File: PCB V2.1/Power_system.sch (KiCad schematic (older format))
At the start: 26 parts, among them J3 B2B-PH-K-S(LF)(SN), J4 B3B-PH-K-S(LF)(SN), Q1 DMG2307L-7, Q2 DMG2307L-7, U2 BQ24210DQCT, U3 AZ1117CR-3.3TRG1_1

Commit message: Images
Images added and organized
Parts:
- added TP35, TP36: TEST_POINT, PCB_Footprints:TEST_POINT, symbol TEST_POINT
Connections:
- wire segments 50 -> 52
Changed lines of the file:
@@
 	5850 2425 5850 3100
 Connection ~ 5850 3100
+$Comp
+L TEST_POINT TP36
+U 1 1 57F5132B
+P 10600 2525
+F 0 "TP36" V 10775 2475 60  0000 L CNN
+F 1 "TEST_POINT" H 10450 2425 60  0000 L CNN
+F 2 "PCB_Footprints:TEST_POINT" H 10775 2800 60  0001 C CNN
+F 3 "" H 10675 2525 60  0001 C CNN
+	1    10600 2525
+	0    -1   -1   0
+$EndComp
+$Comp
+L TEST_POINT TP35
+U 1 1 57F51C69
+P 10150 3700
+F 0 "TP35" V 10325 3650 60  0000 L CNN
+F 1 "TEST_POINT" H 10000 3600 60  0000 L CNN
+F 2 "PCB_Footprints:TEST_POINT" H 10325 3975 60  0001 C CNN
+F 3 "" H 10225 3700 60  0001 C CNN
+	1    10150 3700
+	1    0    0    -1
+$EndComp
+Wire Wire Line
+	10025 3700 10025 3350
+Connection ~ 10025 3350
+Wire Wire Line
+	10600 2650 10600 2900
+Connection ~ 10600 2900
 $EndSCHEMATC

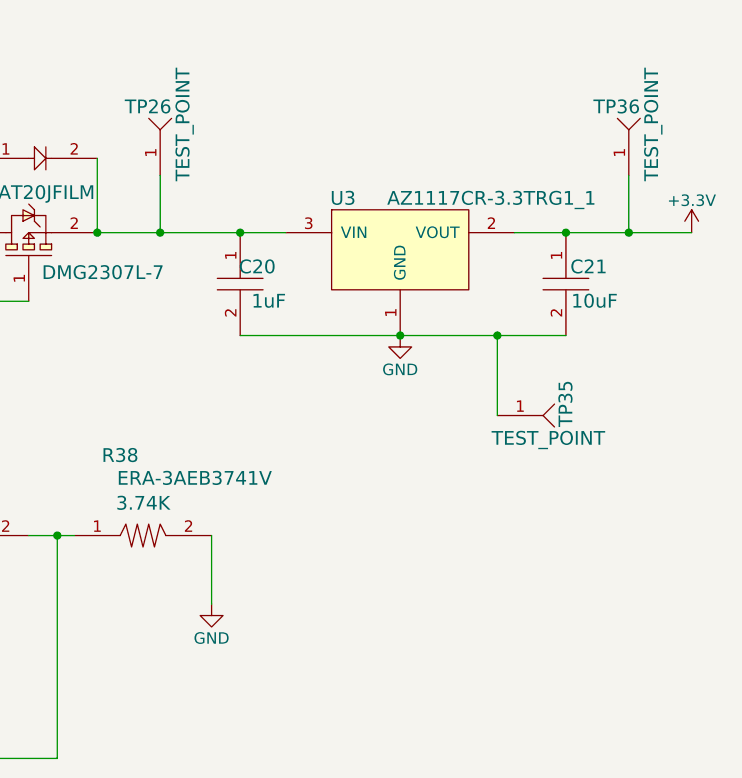
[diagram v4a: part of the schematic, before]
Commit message: LDO and Switch
LDO swapped out for one that better matches the complete system's
amperage requirements. The LDO is now a 600mA one and has a toggle
switch for shuttingit on and off, this will allow the SunLeaf to be
stored and or shipped.
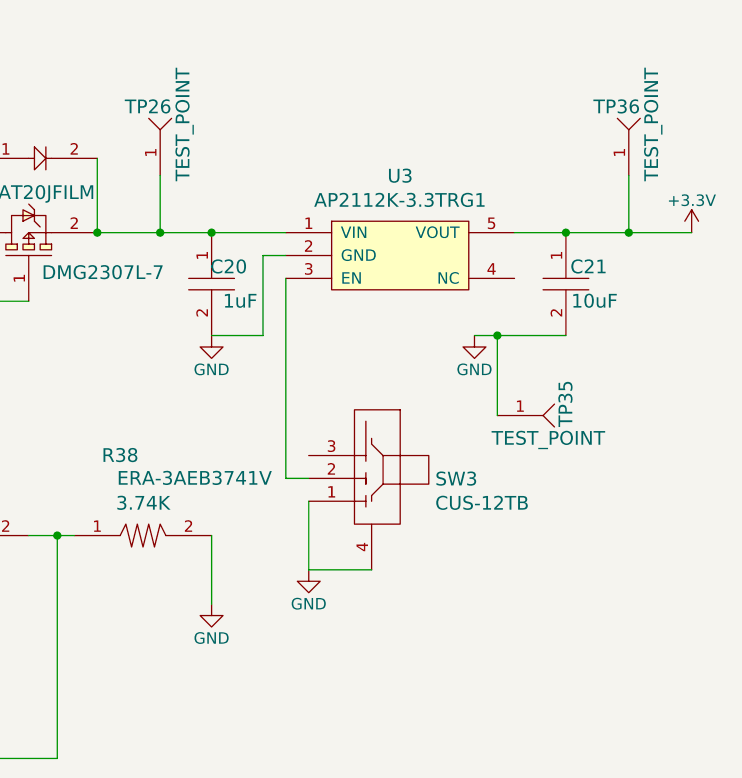
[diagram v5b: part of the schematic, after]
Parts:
- removed U3: AZ1117CR-3.3TRG1_1, PCB_Footprints:AZ1117CR-3.3TRG1, symbol AZ1117CR-3.3TRG1_1
- added SW3: CUS-12TB, PCB_Footprints:CUS-12TB, symbol CUS-12TB
- added U3: AP2112K-3.3TRG1, PCB_Footprints:AP2112K-3.3TRG1, symbol AP2112K-3.3TRG1
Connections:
- wire segments 52 -> 59
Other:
- moved on the sheet: C20
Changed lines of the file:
@@
 L CL05A105KA5NQNC C20
 U 1 1 57D7E6BF
-P 8900 3125
-F 0 "C20" V 8825 3200 60  0000 C CNN
-F 1 "CL05A105KA5NQNC" H 8600 2975 60  0001 C CNN
-F 2 "PCB_Footprints:C0402" H 8150 3175 60  0001 C CNN
-F 3 "http://www.samsungsem.com/kr/support/product-search/mlcc/__icsFiles/afieldfile/2016/08/18/S_CL05A105KA5NQNC.pdf" H 8250 3275 60  0001 C CNN
-F 4 "0.05618 @ 5000" H 8350 3375 60  0001 C CNN "Cost"
-F 5 "5 Sept 2016" H 8450 3475 60  0001 C CNN "Date Created"
-F 6 "5 Sept 2016" H 8550 3575 60  0001 C CNN "Date Modifed"
-F 7 "Adam Vadala-Roth" H 8650 3675 60  0001 C CNN "Designer"
-F 8 "0.55mm" H 8750 3775 60  0001 C CNN "Height"
-F 9 "Yes" H 8850 3875 60  0001 C CNN "RHoS?"
-F 10 "Samsung Electro-Mechanics America, Inc." H 8950 3975 60  0001 C CNN "MFR"
-F 11 "CL05A105KA5NQNC" H 9050 4075 60  0001 C CNN "MFR#"
-F 12 "SMT/SMD" H 9150 4175 60  0001 C CNN "Mounting"
-F 13 "2" H 9250 4275 60  0001 C CNN "Pin Count#"
-F 14 "Active" H 9350 4375 60  0001 C CNN "Status"
-F 15 "10%" H 9450 4475 60  0001 C CNN "Tolerance"
-F 16 "Ceramic Capacitor 0402" H 9550 4575 60  0001 C CNN "Type"
-F 17 "25V" H 9650 4675 60  0001 C CNN "Voltage"
-F 18 "N/A" H 10200 4675 60  0001 C CNN "Wattage"
-F 19 "1uF" V 8975 3250 60  0000 C CNN "Componen-Value"
-F 20 "1µF 25V Ceramic Capacitor X5R 0402 (1005 Metric) 0.039\" L x 0.020\" W (1.00mm x 0.50mm)" H 10400 4875 60  0001 C CNN "Description"
-	1    8900 3125
+P 8775 3125
+F 0 "C20" V 8700 3200 60  0000 C CNN
+F 1 "CL05A105KA5NQNC" H 8475 2975 60  0001 C CNN
+F 2 "PCB_Footprints:C0402" H 8025 3175 60  0001 C CNN
+F 3 "http://www.samsungsem.com/kr/support/product-search/mlcc/__icsFiles/afieldfile/2016/08/18/S_CL05A105KA5NQNC.pdf" H 8125 3275 60  0001 C CNN
+F 4 "0.05618 @ 5000" H 8225 3375 60  0001 C CNN "Cost"
+F 5 "5 Sept 2016" H 8325 3475 60  0001 C CNN "Date Created"
+F 6 "5 Sept 2016" H 8425 3575 60  0001 C CNN "Date Modifed"
+F 7 "Adam Vadala-Roth" H 8525 3675 60  0001 C CNN "Designer"
+F 8 "0.55mm" H 8625 3775 60  0001 C CNN "Height"
+F 9 "Yes" H 8725 3875 60  0001 C CNN "RHoS?"
+F 10 "Samsung Electro-Mechanics America, Inc." H 8825 3975 60  0001 C CNN "MFR"
+F 11 "CL05A105KA5NQNC" H 8925 4075 60  0001 C CNN "MFR#"
+F 12 "SMT/SMD" H 9025 4175 60  0001 C CNN "Mounting"
+F 13 "2" H 9125 4275 60  0001 C CNN "Pin Count#"
+F 14 "Active" H 9225 4375 60  0001 C CNN "Status"
+F 15 "10%" H 9325 4475 60  0001 C CNN "Tolerance"
+F 16 "Ceramic Capacitor 0402" H 9425 4575 60  0001 C CNN "Type"
+F 17 "25V" H 9525 4675 60  0001 C CNN "Voltage"
+F 18 "N/A" H 10075 4675 60  0001 C CNN "Wattage"
+F 19 "1uF" V 8850 3250 60  0000 C CNN "Componen-Value"
+F 20 "1µF 25V Ceramic Capacitor X5R 0402 (1005 Metric) 0.039\" L x 0.020\" W (1.00mm x 0.50mm)" H 10275 4875 60  0001 C CNN "Description"
+	1    8775 3125
 	0    1    1    0
 $EndComp
@@
 $EndComp
 $Comp
-L AZ1117CR-3.3TRG1_1 U3
-U 1 1 57D7E887
-P 9600 2950
-F 0 "U3" H 9350 3150 60  0000 C CNN
-F 1 "AZ1117CR-3.3TRG1_1" H 10000 3150 60  0000 C CNN
-F 2 "PCB_Footprints:AZ1117CR-3.3TRG1" H 9250 3050 60  0001 C CNN
-F 3 "" H 9350 3150 60  0001 C CNN
-F 4 "0.08330 @ 5000" H 9450 3250 60  0001 C CNN "Cost"
-F 5 "19 Aug 2016" H 9550 3350 60  0001 C CNN "Date Created"
-F 6 "19 Aug 2016" H 9650 3450 60  0001 C CNN "Date Modified"
-F 7 "Adam Vadala-Roth" H 9750 3550 60  0001 C CNN "Designer"
-F 8 "1.6mm" H 9850 3650 60  0001 C CNN "Height"
-F 9 "Yes" H 9950 3750 60  0001 C CNN "RHoS?"
-F 10 "Diodes Inc" H 10050 3850 60  0001 C CNN "MFR"
-F 11 "AZ1117CR-3.3TRG1" H 10150 3950 60  0001 C CNN "MFR#"
-F 12 "SMT/SMD" H 10250 4050 60  0001 C CNN "Mounting"
-F 13 "4" H 10350 4150 60  0001 C CNN "Pin Count#"
-F 14 "Active" H 10450 4250 60  0001 C CNN "Status"
-F 15 "N/A" H 10550 4350 60  0001 C CNN "Tolerance"
-F 16 "LDO Linear DC Voltage Regulator" H 10650 4450 60  0001 C CNN "Type"
-F 17 "3.7V input 3.3V Output" H 10750 4550 60  0001 C CNN "Voltage"
-F 18 "N/A" H 10850 4650 60  0001 C CNN "Wattage"
-F 19 "N/A" H 10950 4750 60  0001 C CNN "Component-Value"
-F 20 "Linear Voltage Regulator IC Positive Fixed 1 Output 3.3V 800mA SOT-89" H 11050 4850 60  0001 C CNN "Description"
-	1    9600 2950
-	1    0    0    -1
-$EndComp
-$Comp
 L BAT20JFILM D1
 U 1 1 57D7E99D
@@
 $EndComp
 $Comp
-L +3.3V #PWR40
+L +3.3V #PWR42
 U 1 1 57D80E79
 P 10875 2900
-F 0 "#PWR40" H 10875 2750 50  0001 C CNN
+F 0 "#PWR42" H 10875 2750 50  0001 C CNN
 F 1 "+3.3V" H 10875 3040 50  0000 C CNN
 F 2 "" H 10875 2900 50  0000 C CNN
@@
 $EndComp
 $Comp
-L GND #PWR39
+L GND #PWR38
 U 1 1 57D80F19
-P 9600 3350
-F 0 "#PWR39" H 9600 3100 50  0001 C CNN
-F 1 "GND" H 9600 3200 50  0000 C CNN
-F 2 "" H 9600 3350 50  0000 C CNN
-F 3 "" H 9600 3350 50  0000 C CNN
-	1    9600 3350
+P 8775 3350
+F 0 "#PWR38" H 8775 3100 50  0001 C CNN
+F 1 "GND" H 8775 3200 50  0000 C CNN
+F 2 "" H 8775 3350 50  0000 C CNN
+F 3 "" H 8775 3350 50  0000 C CNN
+	1    8775 3350
 	1    0    0    -1
 $EndComp
@@
 $EndComp
 $Comp
-L GND #PWR38
+L GND #PWR39
 U 1 1 57E05471
 P 8775 4525
-F 0 "#PWR38" H 8775 4275 50  0001 C CNN
+F 0 "#PWR39" H 8775 4275 50  0001 C CNN
 F 1 "GND" H 8775 4375 50  0000 C CNN
 F 2 "" H 8775 4525 50  0000 C CNN
@@
 	10100 2900 10875 2900
 Connection ~ 10325 2900
-Wire Wire Line
-	8900 3350 10325 3350
-Connection ~ 9600 3350
-Connection ~ 8900 2900
+Connection ~ 8775 2900
 Connection ~ 8275 2900
 Wire Wire Line
@@
 	10600 2650 10600 2900
 Connection ~ 10600 2900
+$Comp
+L AP2112K-3.3TRG1 U3
+U 1 1 5816BF07
+P 9600 3000
+F 0 "U3" H 9600 3347 60  0000 C CNN
+F 1 "AP2112K-3.3TRG1" H 9600 3241 60  0000 C CNN
+F 2 "PCB_Footprints:AP2112K-3.3TRG1" H 11300 5000 60  0001 C CNN
+F 3 "http://www.diodes.com/_files/datasheets/AP2112.pdf" H 9350 3200 60  0001 C CNN
+F 4 "0.11866 @ 1000" H 9450 3300 60  0001 C CNN "Cost"
+F 5 "30 Oct 2016" H 9550 3400 60  0001 C CNN "Date Created"
+F 6 "30 Oct 2016" H 9650 3500 60  0001 C CNN "Date Modified"
+F 7 "Adam Vadala-Roth" H 9750 3600 60  0001 C CNN "Designer"
+F 8 "1.45mm" H 9850 3700 60  0001 C CNN "Height"
+F 9 "Yes" H 9950 3800 60  0001 C CNN "RHoS?"
+F 10 "Diodes Inc" H 10050 3900 60  0001 C CNN "MFR"
+F 11 "AP2112K-3.3TRG1" H 10150 4000 60  0001 C CNN "MFR#"
+F 12 "SMT/SMD" H 10250 4100 60  0001 C CNN "Mounting"
+F 13 "4" H 10350 4200 60  0001 C CNN "Pin Count#"
+F 14 "Active" H 10450 4300 60  0001 C CNN "Status"
+F 15 "N/A" H 10550 4400 60  0001 C CNN "Tolerance"
+F 16 "LDO Linear DC Voltage Regulator" H 10650 4500 60  0001 C CNN "Type"
+F 17 "6V input 3.3V Output" H 10750 4600 60  0001 C CNN "Voltage"
+F 18 "N/A" H 10850 4700 60  0001 C CNN "Wattage"
+F 19 "N/A" H 10950 4800 60  0001 C CNN "Component-Value"
+F 20 "Linear Voltage Regulator IC Positive Fixed 1 Output 3.3V 600mA SOT-23-5" H 11050 4900 60  0001 C CNN "Description"
+	1    9600 3000
+	1    0    0    -1
+$EndComp
+$Comp
+L CUS-12TB SW3
+U 1 1 5816C152
+P 9475 3975
+F 0 "SW3" V 9472 3697 60  0000 R CNN
+F 1 "CUS-12TB" V 9366 3697 60  0000 R CNN
+F 2 "PCB_Footprints:CUS-12TB" H 8725 4950 60  0001 C CNN
+F 3 "http://www.nidec-copal-electronics.com/e/catalog/switch/cus.pdf" H 8825 5050 60  0001 C CNN
+F 4 "0.45329 @ 1000" H 8925 5150 60  0001 C CNN "Cost"
+F 5 "24 Oct 2016" H 9025 5250 60  0001 C CNN "Date Created"
+F 6 "24 Oct 2016" H 9125 5350 60  0001 C CNN "Date Modifed"
+F 7 "Adam Vadala-Roth" H 9225 5450 60  0001 C CNN "Designer"
+F 8 "2mm" H 9325 5550 60  0001 C CNN "Height"
+F 9 "Yes" H 9425 5650 60  0001 C CNN "RHoS?"
+F 10 "Copal Electronics Inc." H 9525 5750 60  0001 C CNN "MFR"
+F 11 "CUS-12TB" H 9625 5850 60  0001 C CNN "MFR#"
+F 12 "SMT/SMD" H 9725 5950 60  0001 C CNN "Mounting"
+F 13 "3" H 9825 6050 60  0001 C CNN "Pin Count#"
+F 14 "Active" H 9925 6150 60  0001 C CNN "Status"
+F 15 "N/A" H 10025 6250 60  0001 C CNN "Tolerance"
+F 16 "SMT Slider switch SPDT" H 10125 6350 60  0001 C CNN "Type"
+F 17 "50V 100mA" H 10225 6450 60  0001 C CNN "Voltage"
+F 18 "N/A" H 10775 6450 60  0001 C CNN "Wattage"
+F 19 "N/A" H 9175 4850 60  0001 C CNN "Componen-Value"
+F 20 "Slide Switch SPDT Surface Mount, Right Angle" H 10975 6650 60  0001 C CNN "Description"
+	1    9475 3975
+	0    -1   -1   0
+$EndComp
+Wire Wire Line
+	9925 3350 10325 3350
+$Comp
+L GND #PWR41
+U 1 1 5816D740
+P 9925 3350
+F 0 "#PWR41" H 9925 3100 50  0001 C CNN
+F 1 "GND" H 9925 3200 50  0000 C CNN
+F 2 "" H 9925 3350 50  0000 C CNN
+F 3 "" H 9925 3350 50  0000 C CNN
+	1    9925 3350
+	1    0    0    -1
+$EndComp
+Wire Wire Line
+	9100 3000 9000 3000
+Wire Wire Line
+	9000 3000 9000 3350
+Wire Wire Line
+	9000 3350 8775 3350
+Wire Wire Line
+	9200 4075 9200 4375
+Wire Wire Line
+	9200 4375 9475 4375
+$Comp
+L GND #PWR40
+U 1 1 5816E5B4
+P 9200 4375
+F 0 "#PWR40" H 9200 4125 50  0001 C CNN
+F 1 "GND" H 9200 4225 50  0000 C CNN
+F 2 "" H 9200 4375 50  0000 C CNN
+F 3 "" H 9200 4375 50  0000 C CNN
+	1    9200 4375
+	1    0    0    -1
+$EndComp
+Wire Wire Line
+	9100 3100 9100 3975
+Wire Wire Line
+	9100 3975 9200 3975
 $EndSCHEMATC
